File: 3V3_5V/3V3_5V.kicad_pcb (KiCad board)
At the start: 2 copper layers, 50 x 50 mm, 24 parts, among them J101 USB_C_Receptacle_PowerOnly_6P, J102 Conn_01x02_Pin, J103 Conn_01x02_Pin, U101 LTM4644EY-1-PBF

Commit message: edit schematic and PCB layout
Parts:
- removed R106, R108: 60.4k, Resistor_SMD:R_0603_1608Metric
- removed R107, R109: 13.3k, Resistor_SMD:R_0603_1608Metric
- added C111: 1n, Capacitor_SMD:C_0603_1608Metric, F.Cu at (69.5, 58.5)
- added C112: 1n, Capacitor_SMD:C_0603_1608Metric, F.Cu at (63.5, 66.5)
- C102: renamed from C105; value 220uF -> 47uF; moved to B.Cu
- C103: renamed from C106; value 220uF -> 47uF; moved to B.Cu
- C104: renamed from C107; value 10uF -> 22uF
- C105: renamed from C108; value 10uF -> 22uF
- C107: renamed from C113; value 220uF -> 47uF; moved to B.Cu
- C108: renamed from C114; value 220uF -> 47uF; moved to B.Cu
- C109: renamed from C115; value 10uF -> 22uF
- C110: renamed from C116; value 10uF -> 22uF
- U101: moved to B.Cu
- moved C105 26.4 mm to (81.2, 62.2)
- moved C106 26.1 mm to (63.5, 70.2)
- moved C103 25.9 mm to (81.5, 62.2)
- moved R101 23.0 mm to (64.0, 61.8), turned to 180 degrees
- moved C109 21.8 mm to (81.5, 70.2)
- moved C107 21.5 mm to (81.5, 70.2)
- moved C104 21.3 mm to (81.2, 65.8)
- moved R105 21.2 mm to (67.2, 90.5), turned to -90 degrees
- moved C108 20.9 mm to (81.5, 74.2)
- moved C110 20.6 mm to (81.5, 74.2)
- moved C101 19.8 mm to (63.5, 74.2)
- moved C102 19.4 mm to (81.5, 65.8)
- moved R103 16.6 mm to (67.2, 86.5), turned to -90 degrees
- moved R104 11.0 mm to (81.8, 89.7), turned to -90 degrees
- moved J103 8.70 mm to (96.8, 77.8)
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- renumbered C117 to C101, C118 to C106, R104 to R103, R103 to R104
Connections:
- net /PG3 renamed /PG2
- U101 pad B7: /COMP1 -> /COMP
- U101 pad C4: unconnected-(U101-INTVCC1-PadC4) -> /INTVcc1
- U101 pad E7: /COMP1 -> /COMP
- U101 pad F4: unconnected-(U101-INTVCC2-PadF4) -> /INTVcc1
- U101 pad H7: /COMP2 -> /COMP
- U101 pad L7: /COMP2 -> /COMP
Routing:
- net /INTVcc2: track 0.00 -> 1.80 mm
- net /PG1: track 0.00 -> 1.27 mm
- added copper zone on B.Cu, net +3.3VB

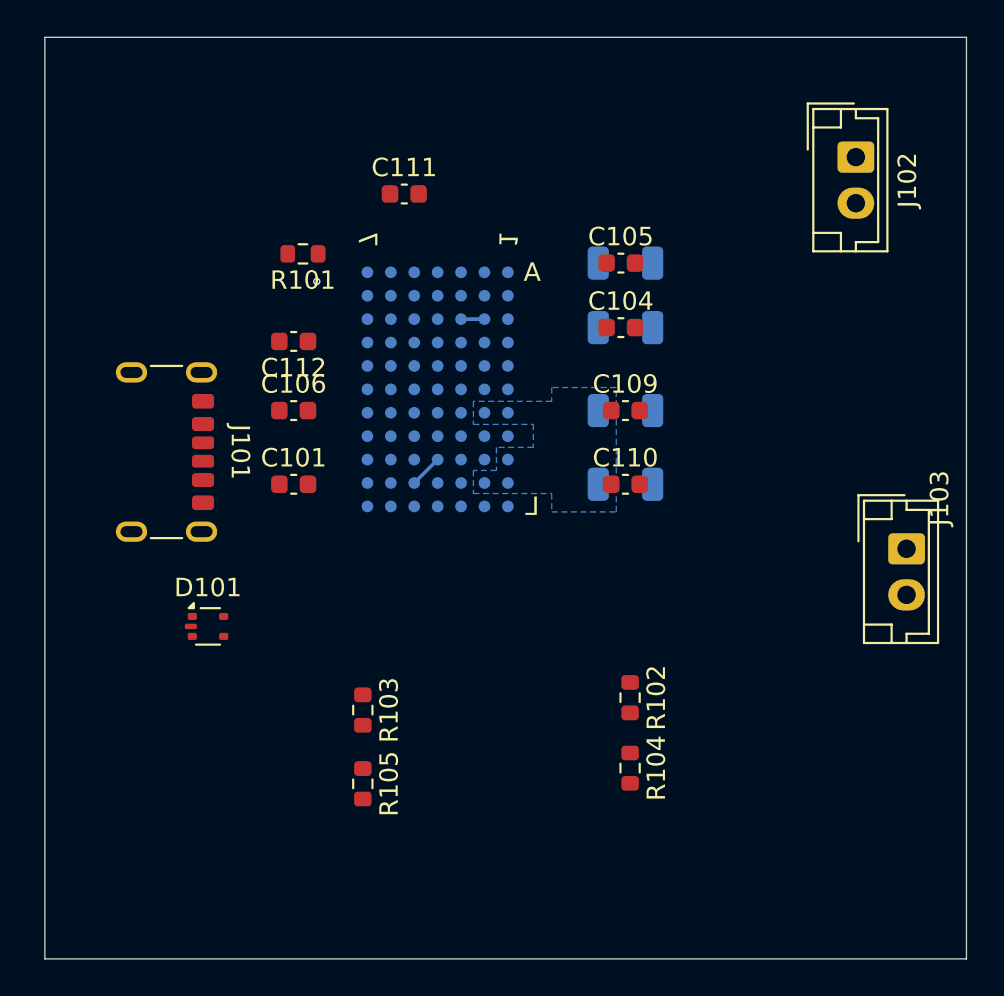
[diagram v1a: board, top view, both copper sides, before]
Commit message: add to sch and pcb
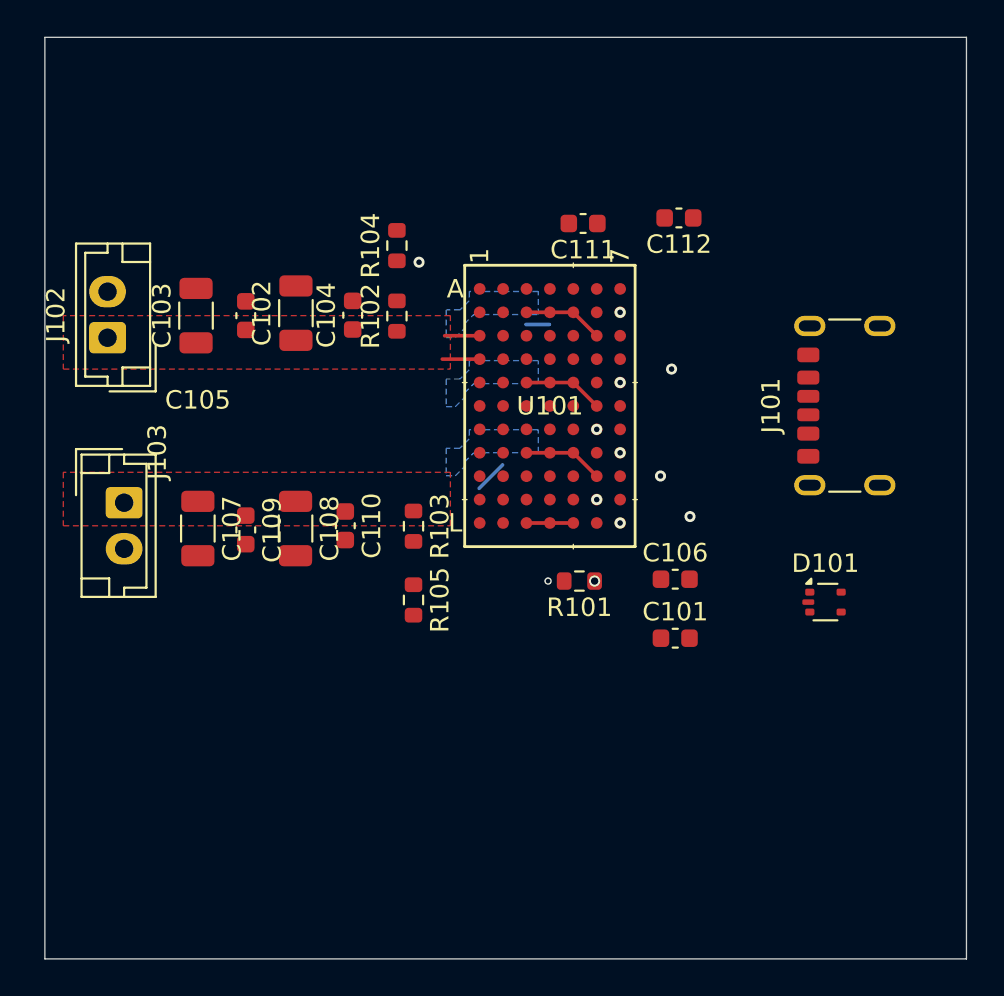
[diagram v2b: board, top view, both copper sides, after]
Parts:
- C102, C103, C107, C108, U101: moved to F.Cu
- moved J103 42.5 mm to (54.3, 75.2)
- moved J102 41.8 mm to (53.4, 66.3), turned to 90 degrees
- moved J101 39.1 mm to (94.5, 70.0), turned to 90 degrees
- moved D101 33.5 mm to (92.3, 80.6)
- moved R104 31.0 mm to (69.1, 61.3), turned to 90 degrees
- moved R102 24.3 mm to (69.1, 65.1), turned to 90 degrees
- moved C107 24.1 mm to (58.3, 76.7), turned to -90 degrees
- moved C103 23.5 mm to (58.2, 65.1), turned to 90 degrees
- moved R101 23.2 mm to (79.0, 79.5)
- moved C106 22.6 mm to (84.2, 79.4)
- moved C101 22.3 mm to (84.2, 82.6)
- moved C112 21.9 mm to (84.4, 59.8)
- moved C109 21.6 mm to (60.9, 76.7), turned to -90 degrees
- moved C105 20.5 mm to (60.9, 65.1), turned to 90 degrees
- moved C108 18.1 mm to (63.6, 76.7), turned to -90 degrees
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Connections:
- R103 pad 1: /3V3B -> +3.3VB
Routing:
- net /Vin: track 0.00 -> 15.5 mm
- net +3.3VA: track 0.00 -> 3.93 mm
- net /TR2/SS2: vias 0 -> 3
- net /TR1/SS1: vias 0 -> 1
- net /SGND: vias 0 -> 2
- net /FB2: vias 0 -> 1
- net /FB1: vias 0 -> 1
- net /COMP: vias 0 -> 4
- net (no net): vias 1 -> 0
- added copper zone on F.Cu, net +3.3VA
- added copper zone on F.Cu, net +3.3VB
- added copper zone on B.Cu, net /Vin
- removed copper zone on B.Cu, net +3.3VB
